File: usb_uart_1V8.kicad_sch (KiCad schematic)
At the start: 22 parts, among them J1 USB_B_Micro, J2 Conn_01x04_Pin, J3 Conn_01x04_Pin, Q1 MMBT3904, U1 FT232RNL, U2 AP2281-3WG

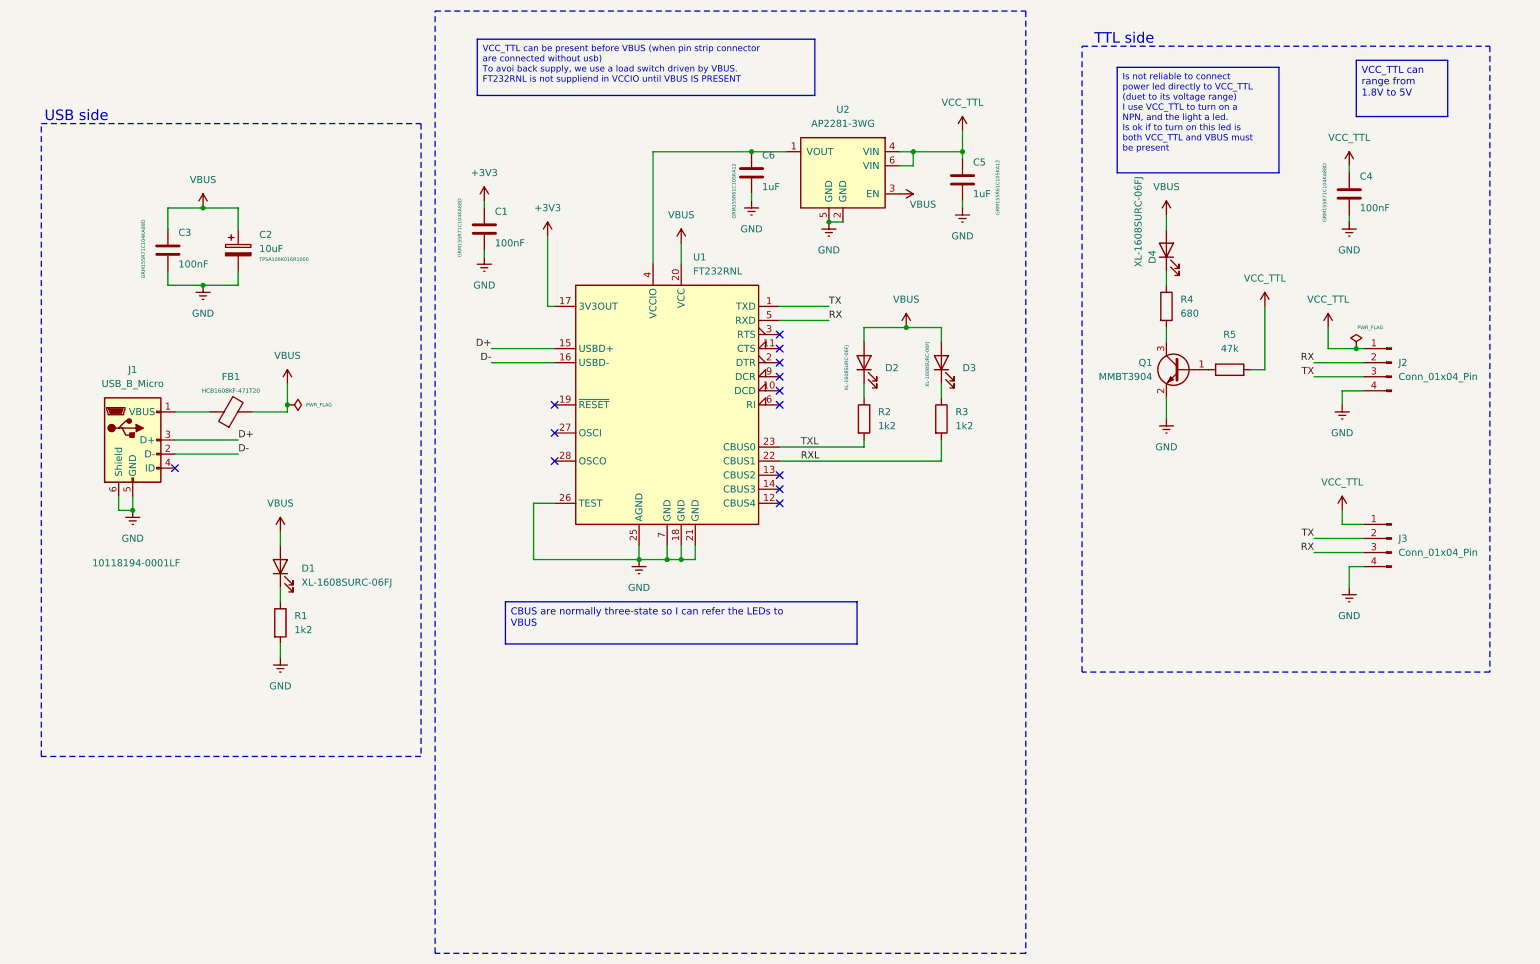
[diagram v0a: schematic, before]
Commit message: [UPG] ft232 supplied by 5V3 and added level shifter
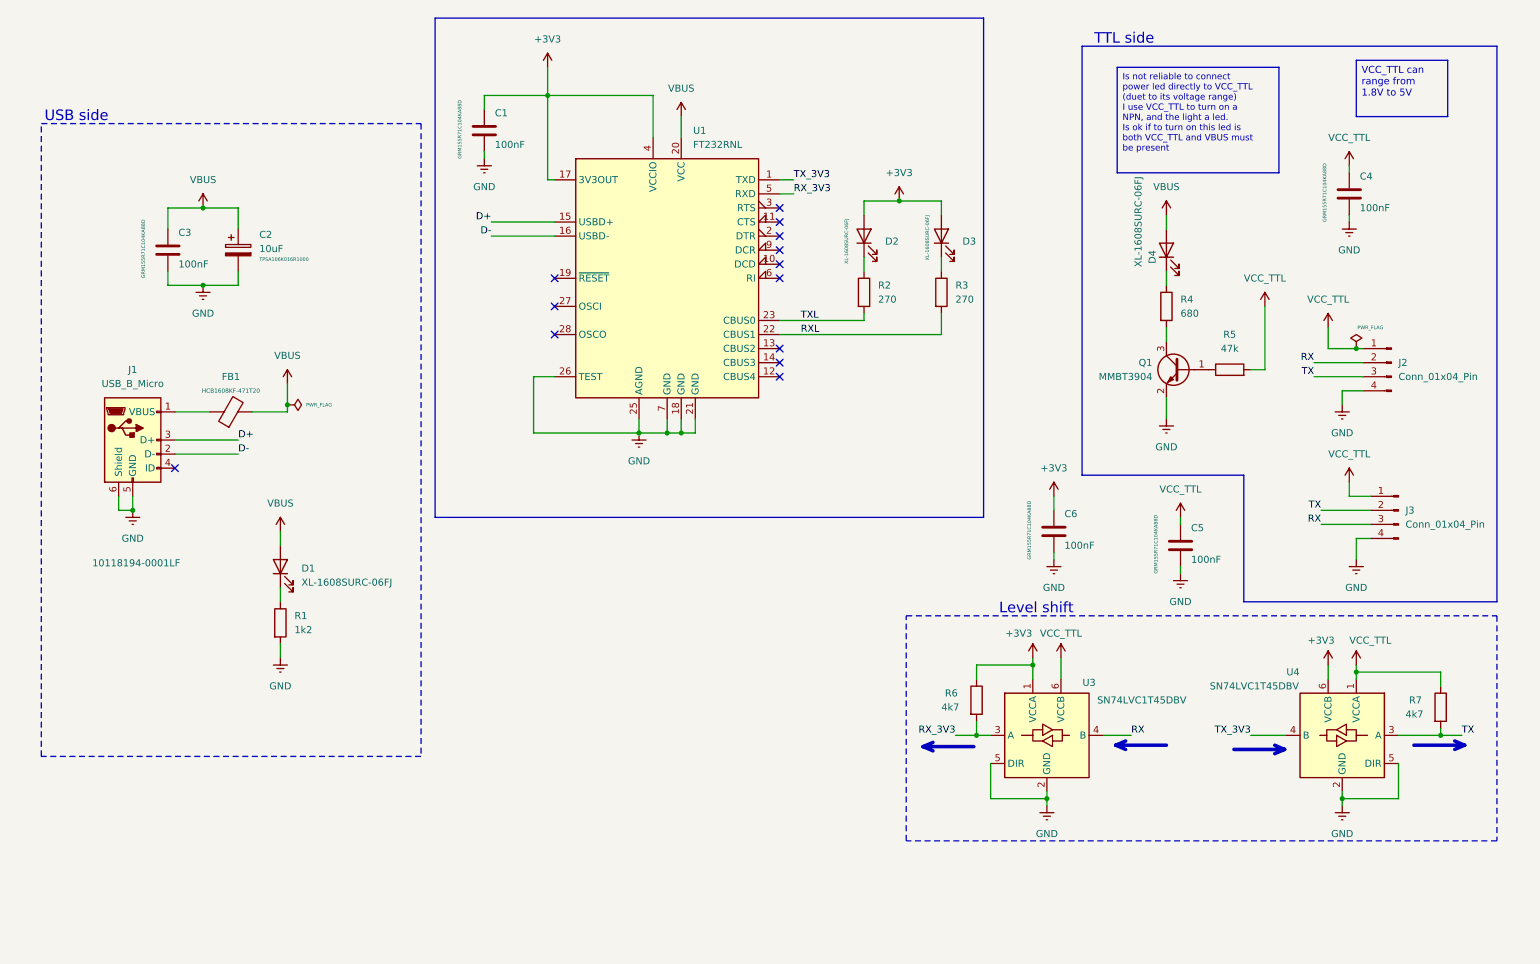
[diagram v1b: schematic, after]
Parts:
- removed U2: AP2281-3WG, Package_TO_SOT_SMD:SOT-23-6, symbol usb_uart_1V8:AP2281-3WG
- added R6, R7: 4k7, Resistor_SMD:R_0402_1005Metric, symbol Device:R
- added U3, U4: SN74LVC1T45DBV, Package_TO_SOT_SMD:SOT-23-6, symbol Logic_LevelTranslator:SN74LVC1T45DBV
- C5, C6: value 1uF -> 100nF; Field6 16V 1uF X5R ±10% 0402 Multilayer Ceramic Capacitors -> (none); JLCPCB Part# C77006 -> C71629
- R2, R3: value 1k2 -> 270; Field6 0402WGF1201TCE -> 0402WGF2700TCE; JLCPCB Part# C25862 -> C25099
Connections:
- net +3V3: now also C6.1, D2.2 (A), D3.2 (A), U1.4 (VCCIO), R6.1, U3.1 (VCCA), U4.6 (VCCB)
- net GND: now also U3.2 (GND), U3.5 (DIR), U4.2 (GND), U4.5 (DIR)
- net RX: now also U3.4 (B); no longer U1.5 (RXD)
- net TX: now also R7.2, U4.3 (A); no longer U1.1 (TXD)
- net VBUS: no longer D2.2 (A), D3.2 (A)
- net VCC_TTL: now also R7.1, U3.6 (VCCB), U4.1 (VCCA)
- new net RX_3V3: R6.2, U1.5 (RXD), U3.3 (A)
- new net TX_3V3: U1.1 (TXD), U4.4 (B)
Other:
- note added: "Level shift"
- moved on the sheet: C1, D2, D3, J3, R2, U1

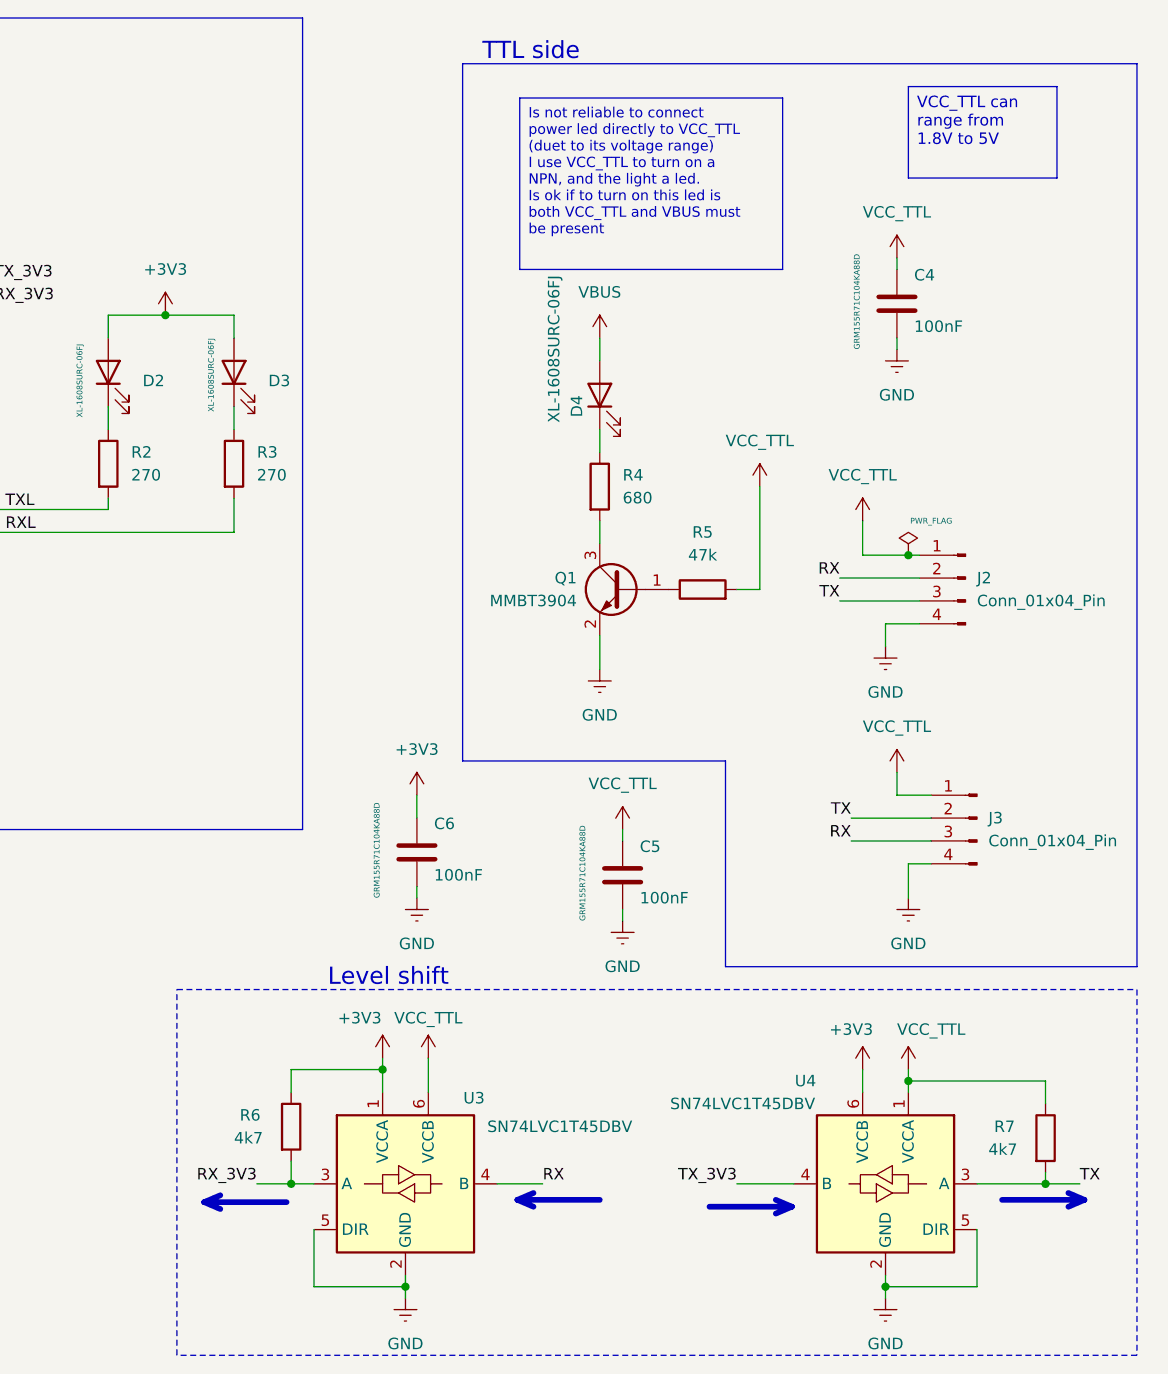
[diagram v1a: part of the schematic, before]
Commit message: [UPG] level shifter: 2 become 1
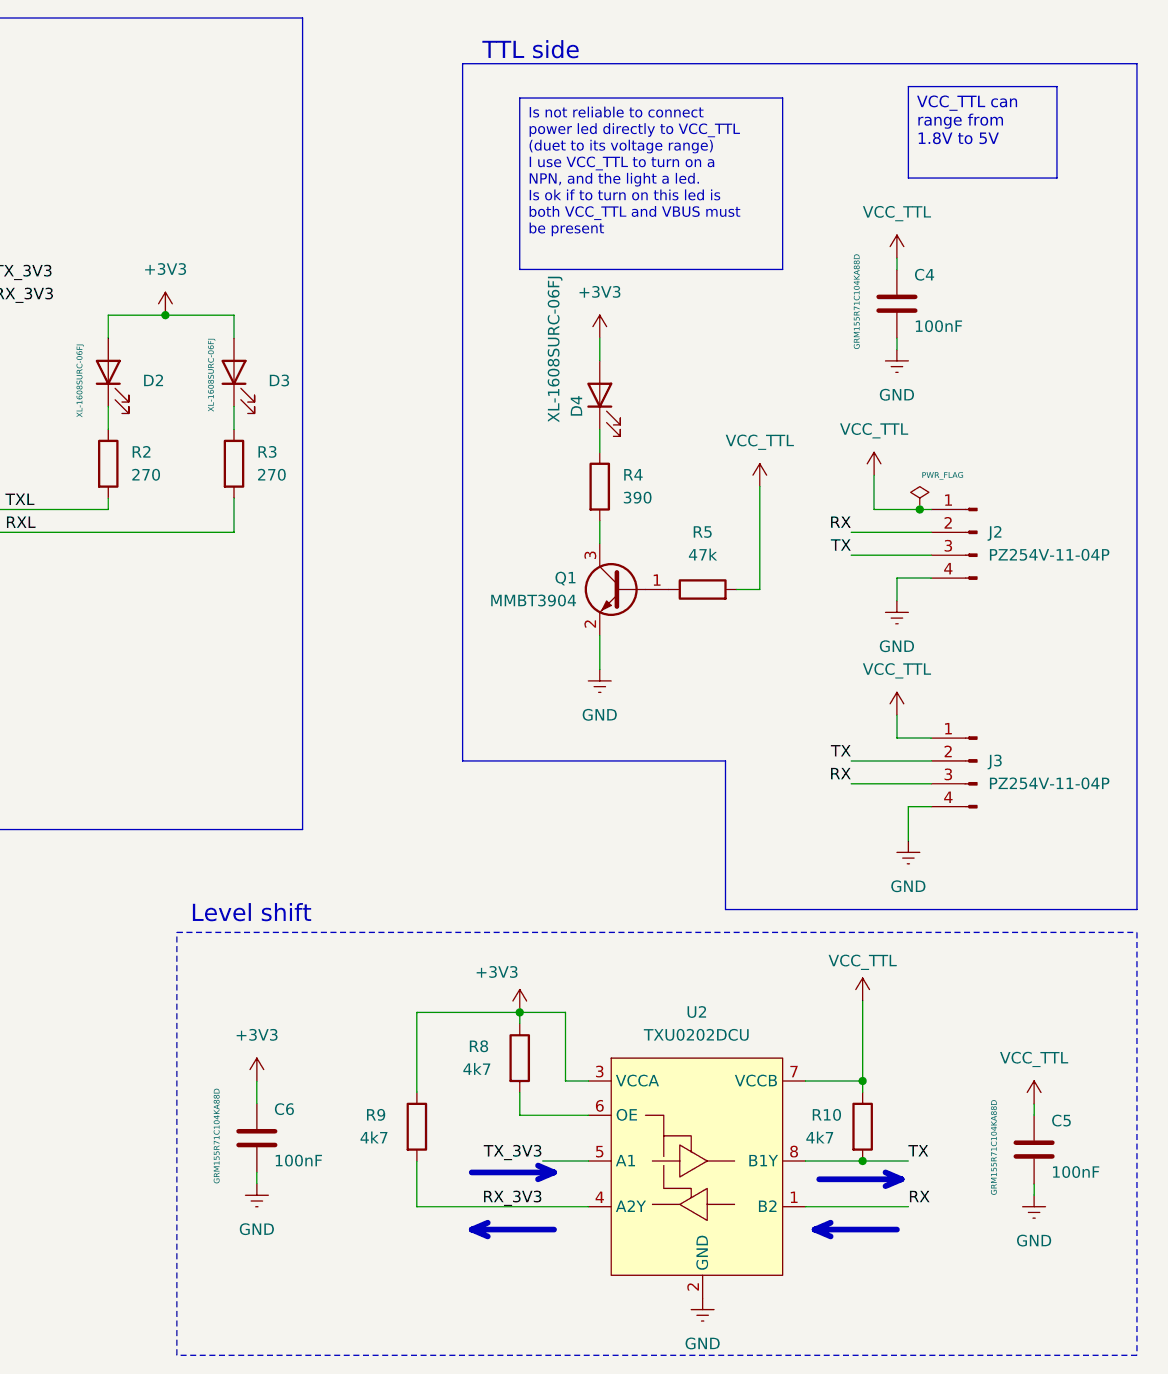
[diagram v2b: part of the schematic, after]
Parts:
- removed R6, R7: 4k7, Resistor_SMD:R_0402_1005Metric, symbol Device:R
- removed U3, U4: SN74LVC1T45DBV, Package_TO_SOT_SMD:SOT-23-6, symbol Logic_LevelTranslator:SN74LVC1T45DBV
- added R10, R8, R9: 4k7, Resistor_SMD:R_0402_1005Metric, symbol Device:R
- added U2: TXU0202DCU, Package_SO:VSSOP-8_2.3x2mm_P0.5mm, symbol usb_uart_1V8:TXU0202DCU
- C1, C3, C4, C5, C6: JLC (none) -> 0402; LCSC (none) -> C71629
- C2: JLC (none) -> CASE-A-3216-18(mm); LCSC (none) -> C282116
- D1, D2, D3, D4: JLC (none) -> 0603; LCSC (none) -> C7371900
- FB1: JLC (none) -> 0603; LCSC (none) -> C356977
- J1: JLC (none) -> SMD; LCSC (none) -> C132563
- J2, J3: value Conn_01x04_Pin -> PZ254V-11-04P; JLC (none) -> Plugin,P=2.54mm; JLCPCB Part# (none) -> C2691448; LCSC (none) -> C2691448
- Q1: JLC (none) -> SOT-23; LCSC (none) -> C7420353
- R1: JLC (none) -> 0402; LCSC (none) -> C25862
- R2, R3: JLC (none) -> 0402; LCSC (none) -> C25099
- R4: value 680 -> 390; Field6 0402WGF6800TCE -> 0402WGJ0391TCE; JLC (none) -> 0402; JLCPCB Part# C25130 -> C25163; LCSC (none) -> C25163
- R5: JLC (none) -> 0402; LCSC (none) -> C25792
- U1: JLC (none) -> SSOP-28; LCSC (none) -> C5246810
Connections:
- net +3V3: now also D4.2 (A), R8.1, R9.1, U2.3 (VCCA)
- net GND: now also U2.2 (GND)
- net RX: now also U2.1 (B2)
- net RX_3V3: now also R9.2, U2.4 (A2Y)
- net TX: now also R10.2, U2.8 (B1Y)
- net TX_3V3: now also U2.5 (A1)
- net VBUS: no longer D4.2 (A)
- net VCC_TTL: now also R10.1, U2.7 (VCCB)
- new net: R8.2, U2.6 (OE)
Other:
- moved on the sheet: C5, C6, J2
